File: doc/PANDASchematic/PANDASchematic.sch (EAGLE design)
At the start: 11 parts, among them IC1 74LS595N, U1 ELECTRIC_IMP

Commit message: Laid out schematic and state transfers
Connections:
- net GND: now also IC1A.G
- net VDD: now also LCD1.VDD
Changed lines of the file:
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@@
 <part name="SUPPLY8" library="supply2" deviceset="GND" device=""/>
 <part name="SUPPLY9" library="supply2" deviceset="GND" device=""/>
+<part name="SUPPLY10" library="supply2" deviceset="GND" device=""/>
+<part name="SUPPLY11" library="SparkFun-Aesthetics" deviceset="VDD" device=""/>
 </parts>
 <sheets>
@@
 <instance part="SUPPLY8" gate="GND" x="76.2" y="68.58"/>
 <instance part="SUPPLY9" gate="GND" x="38.1" y="68.58"/>
+<instance part="SUPPLY10" gate="GND" x="104.14" y="50.8"/>
+<instance part="SUPPLY11" gate="VDD" x="35.56" y="40.64"/>
 </instances>
 <busses>
@@
 <pinref part="SUPPLY9" gate="GND" pin="GND"/>
 </segment>
+<segment>
+<pinref part="IC1" gate="A" pin="G"/>
+<pinref part="SUPPLY10" gate="GND" pin="GND"/>
+<wire x1="104.14" y1="53.34" x2="101.6" y2="53.34" width="0.1524" layer="91"/>
+</segment>
 </net>
 <net name="VDD" class="0">
@@
 <wire x1="104.14" y1="38.1" x2="101.6" y2="38.1" width="0.1524" layer="91"/>
 </segment>
+<segment>
+<pinref part="LCD1" gate="G$1" pin="VDD"/>
+<pinref part="SUPPLY11" gate="VDD" pin="VDD"/>
+<wire x1="35.56" y1="40.64" x2="33.02" y2="40.64" width="0.1524" layer="91"/>
+</segment>
 </net>

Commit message: Updated schematic to match soldered circuit
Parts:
- removed R2: 68Ω, SparkFun-Passives:RESISTORAXIAL-0.3
- added T1: 2N2222, adafruit:2N2222
- LED1, LED2: value TLUV5300 -> LTL-30EFJ
- R4, R5: value 47Ω -> 100Ω
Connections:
- net GND: now also T1.E; no longer R2.2
- net N$10: now also IC1A.QG, LED2.AG; no longer IC1A.QD, LED1.AO
- net N$11: now also IC1A.QF, LED1.AO; no longer IC1A.QE, LED2.AG
- net N$12: now also IC1A.QE, LED1.AG; no longer IC1A.QF, LED2.AO
- net N$13: now also T1.B, U1.1(CLK2/CTS1/TX3/SCL2); no longer R2.1, SG1.2
- net N$3: now also SG1.2, T1.C; no longer SG1.1, U1.1(CLK2/CTS1/TX3/SCL2)
- net N$7: now also IC1A.QC; no longer IC1A.QA
- net N$9: now also IC1A.QH, LED2.AO; no longer IC1A.QC, LED1.AG
- net VDD: now also SG1.1
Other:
- moved on the sheet: SG1
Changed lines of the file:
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@@
 <layer number="230" name="230bmp" color="7" fill="1" visible="yes" active="yes"/>
 <layer number="231" name="231bmp" color="7" fill="1" visible="yes" active="yes"/>
+<layer number="232" name="Eagle3D_PG2" color="7" fill="1" visible="no" active="no"/>
+<layer number="233" name="Eagle3D_PG3" color="7" fill="1" visible="no" active="no"/>
 <layer number="248" name="Housing" color="7" fill="1" visible="yes" active="yes"/>
 <layer number="249" name="Edge" color="7" fill="1" visible="yes" active="yes"/>
@@
 <parts>
 <part name="U1" library="SparkFun-RF" deviceset="ELECTRIC_IMP" device=""/>
-<part name="LED1" library="led" deviceset="TLUV5300" device=""/>
-<part name="LED2" library="led" deviceset="TLUV5300" device=""/>
+<part name="LED1" library="led" deviceset="TLUV5300" device="" value="LTL-30EFJ"/>
+<part name="LED2" library="led" deviceset="TLUV5300" device="" value="LTL-30EFJ"/>
 <part name="LCD1" library="lph-7366" deviceset="LPH-7366" device=""/>
 <part name="IC1" library="74xx-us" deviceset="74*595" device="N" technology="LS"/>
 <part name="SG1" library="SparkFun-Electromechanical" deviceset="BUZZER" device="NS"/>
 <part name="R1" library="SparkFun-Sensors" deviceset="PHOTOCELL" device="PTH"/>
-<part name="R2" library="SparkFun-Passives" deviceset="RESISTOR" device="AXIAL-0.3" value="68Ω"/>
 <part name="R3" library="SparkFun-Passives" deviceset="RESISTOR" device="AXIAL-0.3" value="10kΩ"/>
 <part name="SUPPLY2" library="supply2" deviceset="GND" device=""/>
@@
 <part name="SUPPLY6" library="SparkFun-Aesthetics" deviceset="VDD" device=""/>
 <part name="SUPPLY7" library="SparkFun-Aesthetics" deviceset="VDD" device=""/>
-<part name="R4" library="SparkFun-Passives" deviceset="RESISTOR" device="AXIAL-0.3" value="47Ω"/>
-<part name="R5" library="SparkFun-Passives" deviceset="RESISTOR" device="AXIAL-0.3" value="47Ω"/>
+<part name="R4" library="SparkFun-Passives" deviceset="RESISTOR" device="AXIAL-0.3" value="100Ω"/>
+<part name="R5" library="SparkFun-Passives" deviceset="RESISTOR" device="AXIAL-0.3" value="100Ω"/>
 <part name="SUPPLY8" library="supply2" deviceset="GND" device=""/>
 <part name="SUPPLY9" library="supply2" deviceset="GND" device=""/>
 <part name="SUPPLY10" library="supply2" deviceset="GND" device=""/>
 <part name="SUPPLY11" library="SparkFun-Aesthetics" deviceset="VDD" device=""/>
+<part name="T1" library="adafruit" deviceset="2N2222" device=""/>
+<part name="SUPPLY12" library="SparkFun-Aesthetics" deviceset="VDD" device=""/>
 </parts>
 <sheets>
@@
 <instance part="LCD1" gate="G$1" x="15.24" y="35.56" rot="R180"/>
 <instance part="IC1" gate="A" x="91.44" y="40.64" rot="R180"/>
-<instance part="SG1" gate="G$1" x="121.92" y="40.64"/>
+<instance part="SG1" gate="G$1" x="124.46" y="55.88"/>
 <instance part="R1" gate="G$1" x="73.66" y="5.08" rot="R180"/>
-<instance part="R2" gate="G$1" x="137.16" y="35.56"/>
 <instance part="R3" gate="G$1" x="91.44" y="5.08" rot="R180"/>
 <instance part="SUPPLY2" gate="GND" x="35.56" y="50.8"/>
 <instance part="SUPPLY1" gate="VDD" x="175.26" y="25.4"/>
 <instance part="SUPPLY3" gate="GND" x="175.26" y="7.62"/>
-<instance part="SUPPLY4" gate="GND" x="147.32" y="33.02"/>
+<instance part="SUPPLY4" gate="GND" x="127" y="35.56"/>
 <instance part="SUPPLY5" gate="GND" x="66.04" y="0"/>
 <instance part="SUPPLY6" gate="VDD" x="99.06" y="5.08"/>
 <instance part="SUPPLY7" gate="VDD" x="104.14" y="38.1"/>
 <instance part="R4" gate="G$1" x="43.18" y="71.12" rot="R180"/>
-<instance part="R5" gate="G$1" x="71.12" y="71.12" rot="R180"/>
-<instance part="SUPPLY8" gate="GND" x="76.2" y="68.58"/>
+<instance part="R5" gate="G$1" x="71.12" y="71.12" smashed="yes" rot="R180">
+<attribute name="NAME" x="72.39" y="69.6214" size="1.778" layer="95" rot="R180"/>
+<attribute name="VALUE" x="74.93" y="74.422" size="1.778" layer="96" rot="R180"/>
+</instance>
+<instance part="SUPPLY8" gate="GND" x="76.2" y="68.58" smashed="yes">
+<attribute name="VALUE" x="74.295" y="65.405" size="1.778" layer="96"/>
+</instance>
 <instance part="SUPPLY9" gate="GND" x="38.1" y="68.58"/>
 <instance part="SUPPLY10" gate="GND" x="104.14" y="50.8"/>
 <instance part="SUPPLY11" gate="VDD" x="35.56" y="40.64"/>
+<instance part="T1" gate="G$1" x="124.46" y="45.72" smashed="yes">
+<attribute name="NAME" x="129.54" y="48.26" size="1.778" layer="95"/>
+<attribute name="VALUE" x="129.54" y="45.72" size="1.778" layer="96"/>
+</instance>
+<instance part="SUPPLY12" gate="VDD" x="119.38" y="63.5"/>
 </instances>
 <busses>
@@
 </segment>
 <segment>
-<pinref part="R2" gate="G$1" pin="2"/>
-<pinref part="SUPPLY4" gate="GND" pin="GND"/>
-<wire x1="147.32" y1="35.56" x2="142.24" y2="35.56" width="0.1524" layer="91"/>
-</segment>
-<segment>
 <pinref part="R5" gate="G$1" pin="1"/>
 <pinref part="SUPPLY8" gate="GND" pin="GND"/>
@@
 <wire x1="104.14" y1="53.34" x2="101.6" y2="53.34" width="0.1524" layer="91"/>
 </segment>
+<segment>
+<pinref part="T1" gate="G$1" pin="E"/>
+<pinref part="SUPPLY4" gate="GND" pin="GND"/>
+<wire x1="127" y1="40.64" x2="127" y2="38.1" width="0.1524" layer="91"/>
+</segment>
 </net>
 <net name="VDD" class="0">
@@
 <pinref part="SUPPLY11" gate="VDD" pin="VDD"/>
 <wire x1="35.56" y1="40.64" x2="33.02" y2="40.64" width="0.1524" layer="91"/>
+</segment>
+<segment>
+<pinref part="SUPPLY12" gate="VDD" pin="VDD"/>
+<wire x1="119.38" y1="63.5" x2="119.38" y2="53.34" width="0.1524" layer="91"/>
+<pinref part="SG1" gate="G$1" pin="1"/>
+<wire x1="119.38" y1="53.34" x2="124.46" y2="53.34" width="0.1524" layer="91"/>
 </segment>
 </net>
@@
 </segment>
 </net>
-<net name="N$3" class="0">
-<segment>
-<pinref part="SG1" gate="G$1" pin="1"/>
-<pinref part="U1" gate="G$1" pin="1(CLK2/CTS1/TX3/SCL2)"/>
-<wire x1="121.92" y1="38.1" x2="121.92" y2="25.4" width="0.1524" layer="91"/>
-</segment>
-</net>
-<net name="N$7" class="0">
-<segment>
-<pinref part="LCD1" gate="G$1" pin="/RES"/>
-<pinref part="IC1" gate="A" pin="QA"/>
-<wire x1="33.02" y1="30.48" x2="78.74" y2="30.48" width="0.1524" layer="91"/>
-</segment>
-</net>
 <net name="N$8" class="0">
 <segment>
@@
 <wire x1="48.26" y1="22.86" x2="48.26" y2="33.02" width="0.1524" layer="91"/>
 <pinref part="IC1" gate="A" pin="QB"/>
-<wire x1="48.26" y1="33.02" x2="78.74" y2="33.02" width="0.1524" layer="91"/>
-</segment>
-</net>
-<net name="N$9" class="0">
-<segment>
-<pinref part="IC1" gate="A" pin="QC"/>
-<pinref part="LED1" gate="G$1" pin="AG"/>
-<wire x1="78.74" y1="35.56" x2="40.64" y2="35.56" width="0.1524" layer="91"/>
-<wire x1="40.64" y1="35.56" x2="40.64" y2="60.96" width="0.1524" layer="91"/>
-</segment>
-</net>
-<net name="N$10" class="0">
-<segment>
-<pinref part="LED1" gate="G$1" pin="AO"/>
-<wire x1="55.88" y1="60.96" x2="55.88" y2="38.1" width="0.1524" layer="91"/>
-<pinref part="IC1" gate="A" pin="QD"/>
-<wire x1="55.88" y1="38.1" x2="78.74" y2="38.1" width="0.1524" layer="91"/>
-</segment>
-</net>
-<net name="N$11" class="0">
-<segment>
-<pinref part="LED2" gate="G$1" pin="AG"/>
-<wire x1="58.42" y1="60.96" x2="58.42" y2="40.64" width="0.1524" layer="91"/>
-<pinref part="IC1" gate="A" pin="QE"/>
-<wire x1="58.42" y1="40.64" x2="78.74" y2="40.64" width="0.1524" layer="91"/>
-</segment>
-</net>
-<net name="N$12" class="0">
-<segment>
-<pinref part="LED2" gate="G$1" pin="AO"/>
-<wire x1="73.66" y1="60.96" x2="73.66" y2="43.18" width="0.1524" layer="91"/>
-<pinref part="IC1" gate="A" pin="QF"/>
-<wire x1="73.66" y1="43.18" x2="78.74" y2="43.18" width="0.1524" layer="91"/>
-</segment>
-</net>
-<net name="N$13" class="0">
-<segment>
-<pinref part="SG1" gate="G$1" pin="2"/>
-<pinref part="R2" gate="G$1" pin="1"/>
-<wire x1="132.08" y1="35.56" x2="124.46" y2="35.56" width="0.1524" layer="91"/>
-<wire x1="124.46" y1="35.56" x2="124.46" y2="38.1" width="0.1524" layer="91"/>
+<wire x1="78.74" y1="33.02" x2="48.26" y2="33.02" width="0.1524" layer="91"/>
 </segment>
 </net>
@@
 </segment>
 </net>
+<net name="N$3" class="0">
+<segment>
+<pinref part="SG1" gate="G$1" pin="2"/>
+<pinref part="T1" gate="G$1" pin="C"/>
+<wire x1="127" y1="53.34" x2="127" y2="50.8" width="0.1524" layer="91"/>
+</segment>
+</net>
+<net name="N$13" class="0">
+<segment>
+<pinref part="T1" gate="G$1" pin="B"/>
+<pinref part="U1" gate="G$1" pin="1(CLK2/CTS1/TX3/SCL2)"/>
+<wire x1="121.92" y1="45.72" x2="121.92" y2="25.4" width="0.1524" layer="91"/>
+</segment>
+</net>
+<net name="N$7" class="0">
+<segment>
+<pinref part="LCD1" gate="G$1" pin="/RES"/>
+<wire x1="33.02" y1="30.48" x2="45.72" y2="30.48" width="0.1524" layer="91"/>
+<wire x1="45.72" y1="30.48" x2="45.72" y2="35.56" width="0.1524" layer="91"/>
+<pinref part="IC1" gate="A" pin="QC"/>
+<wire x1="45.72" y1="35.56" x2="78.74" y2="35.56" width="0.1524" layer="91"/>
+</segment>
+</net>
+<net name="N$9" class="0">
+<segment>
+<pinref part="LED2" gate="G$1" pin="AO"/>
+<wire x1="73.66" y1="60.96" x2="73.66" y2="48.26" width="0.1524" layer="91"/>
+<pinref part="IC1" gate="A" pin="QH"/>
+<wire x1="73.66" y1="48.26" x2="78.74" y2="48.26" width="0.1524" layer="91"/>
+</segment>
+</net>
+<net name="N$10" class="0">
+<segment>
+<pinref part="LED2" gate="G$1" pin="AG"/>
+<wire x1="58.42" y1="60.96" x2="58.42" y2="45.72" width="0.1524" layer="91"/>
+<pinref part="IC1" gate="A" pin="QG"/>
+<wire x1="58.42" y1="45.72" x2="78.74" y2="45.72" width="0.1524" layer="91"/>
+</segment>
+</net>
+<net name="N$11" class="0">
+<segment>
+<pinref part="LED1" gate="G$1" pin="AO"/>
+<wire x1="55.88" y1="60.96" x2="55.88" y2="43.18" width="0.1524" layer="91"/>
+<pinref part="IC1" gate="A" pin="QF"/>
+<wire x1="55.88" y1="43.18" x2="78.74" y2="43.18" width="0.1524" layer="91"/>
+</segment>
+</net>
+<net name="N$12" class="0">
+<segment>
+<pinref part="IC1" gate="A" pin="QE"/>
+<wire x1="40.64" y1="40.64" x2="78.74" y2="40.64" width="0.1524" layer="91"/>
+<pinref part="LED1" gate="G$1" pin="AG"/>
+<wire x1="40.64" y1="60.96" x2="40.64" y2="40.64" width="0.1524" layer="91"/>
+</segment>
+</net>

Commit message: Updated documentation, added series resistors to SCL/MOSI lines
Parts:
- added R2, R6: 68Ω, SparkFun-Passives:RESISTORAXIAL-0.3
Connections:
- new net N$16: LCD1.SCLK, R2.2
- new net N$17: LCD1.SDIN, R6.2
- net N$1: now also R6.1; no longer LCD1.SDIN
- net N$2: now also R2.1; no longer LCD1.SCLK
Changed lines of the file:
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@@
 <part name="T1" library="adafruit" deviceset="2N2222" device=""/>
 <part name="SUPPLY12" library="SparkFun-Aesthetics" deviceset="VDD" device=""/>
+<part name="R2" library="SparkFun-Passives" deviceset="RESISTOR" device="AXIAL-0.3" value="68Ω"/>
+<part name="R6" library="SparkFun-Passives" deviceset="RESISTOR" device="AXIAL-0.3" value="68Ω"/>
 </parts>
 <sheets>
@@
 </instance>
 <instance part="SUPPLY12" gate="VDD" x="119.38" y="63.5"/>
+<instance part="R2" gate="G$1" x="58.42" y="20.32" rot="R180"/>
+<instance part="R6" gate="G$1" x="71.12" y="17.78" rot="R180"/>
 </instances>
 <busses>
@@
 <net name="N$2" class="0">
 <segment>
-<pinref part="LCD1" gate="G$1" pin="SCLK"/>
 <pinref part="U1" gate="G$1" pin="5(SCLK1/SCLK2/TX2)"/>
-<wire x1="33.02" y1="20.32" x2="106.68" y2="20.32" width="0.1524" layer="91"/>
 <pinref part="IC1" gate="A" pin="SCK"/>
 <wire x1="106.68" y1="20.32" x2="121.92" y2="20.32" width="0.1524" layer="91"/>
 <wire x1="101.6" y1="35.56" x2="106.68" y2="35.56" width="0.1524" layer="91"/>
 <wire x1="106.68" y1="35.56" x2="106.68" y2="20.32" width="0.1524" layer="91"/>
+<pinref part="R2" gate="G$1" pin="1"/>
+<wire x1="63.5" y1="20.32" x2="106.68" y2="20.32" width="0.1524" layer="91"/>
 <junction x="106.68" y="20.32"/>
 </segment>
@@
 <pinref part="IC1" gate="A" pin="SER"/>
 <wire x1="101.6" y1="30.48" x2="104.14" y2="30.48" width="0.1524" layer="91"/>
-<pinref part="LCD1" gate="G$1" pin="SDIN"/>
 <pinref part="U1" gate="G$1" pin="7(MOSI1/MISO2/RX2)"/>
-<wire x1="33.02" y1="17.78" x2="104.14" y2="17.78" width="0.1524" layer="91"/>
 <wire x1="104.14" y1="17.78" x2="121.92" y2="17.78" width="0.1524" layer="91"/>
 <wire x1="104.14" y1="30.48" x2="104.14" y2="17.78" width="0.1524" layer="91"/>
+<pinref part="R6" gate="G$1" pin="1"/>
+<wire x1="76.2" y1="17.78" x2="104.14" y2="17.78" width="0.1524" layer="91"/>
 <junction x="104.14" y="17.78"/>
 </segment>
@@
 </segment>
 </net>
+<net name="N$16" class="0">
+<segment>
+<pinref part="LCD1" gate="G$1" pin="SCLK"/>
+<pinref part="R2" gate="G$1" pin="2"/>
+<wire x1="33.02" y1="20.32" x2="53.34" y2="20.32" width="0.1524" layer="91"/>
+</segment>
+</net>
+<net name="N$17" class="0">
+<segment>
+<pinref part="LCD1" gate="G$1" pin="SDIN"/>
+<pinref part="R6" gate="G$1" pin="2"/>
+<wire x1="33.02" y1="17.78" x2="66.04" y2="17.78" width="0.1524" layer="91"/>
+</segment>
+</net>

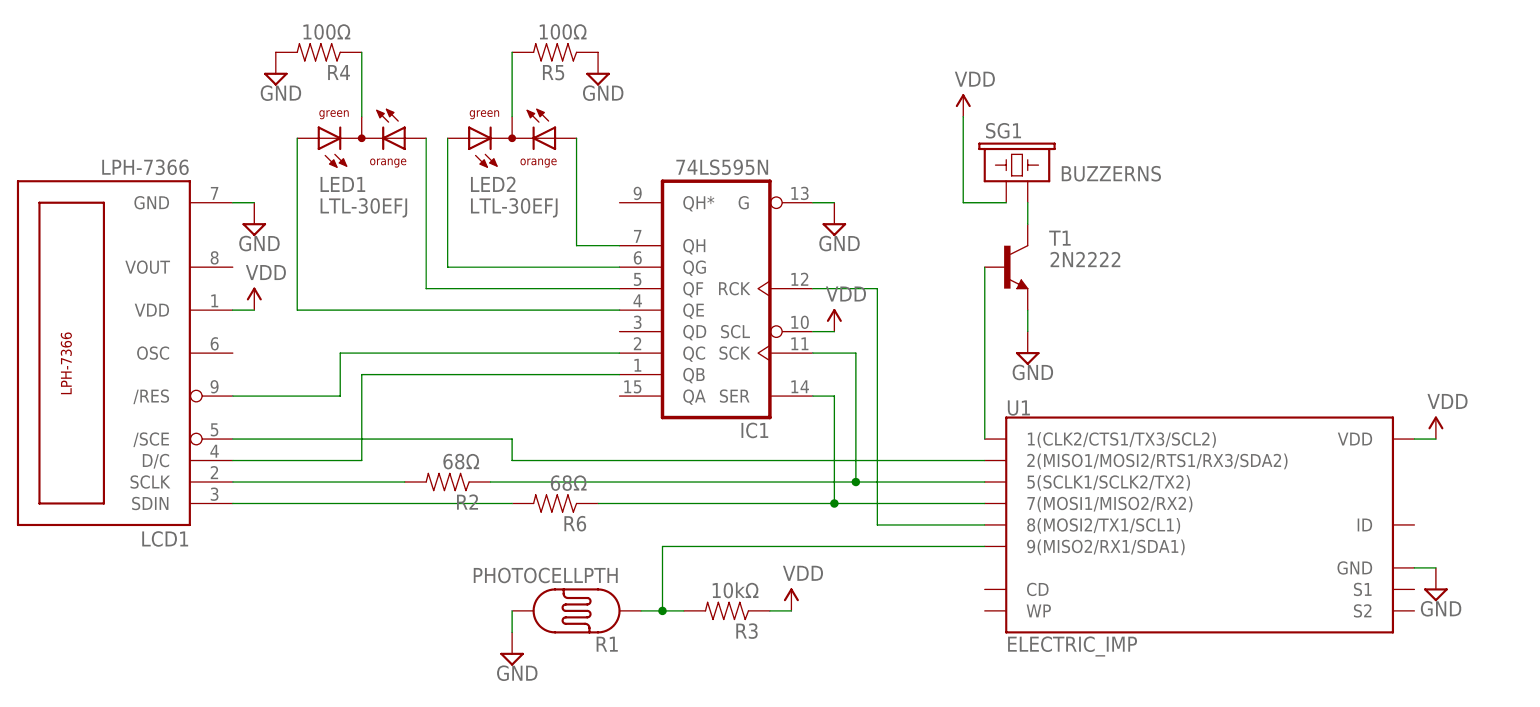
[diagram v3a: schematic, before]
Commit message: Updated schematic to 3 LEDs
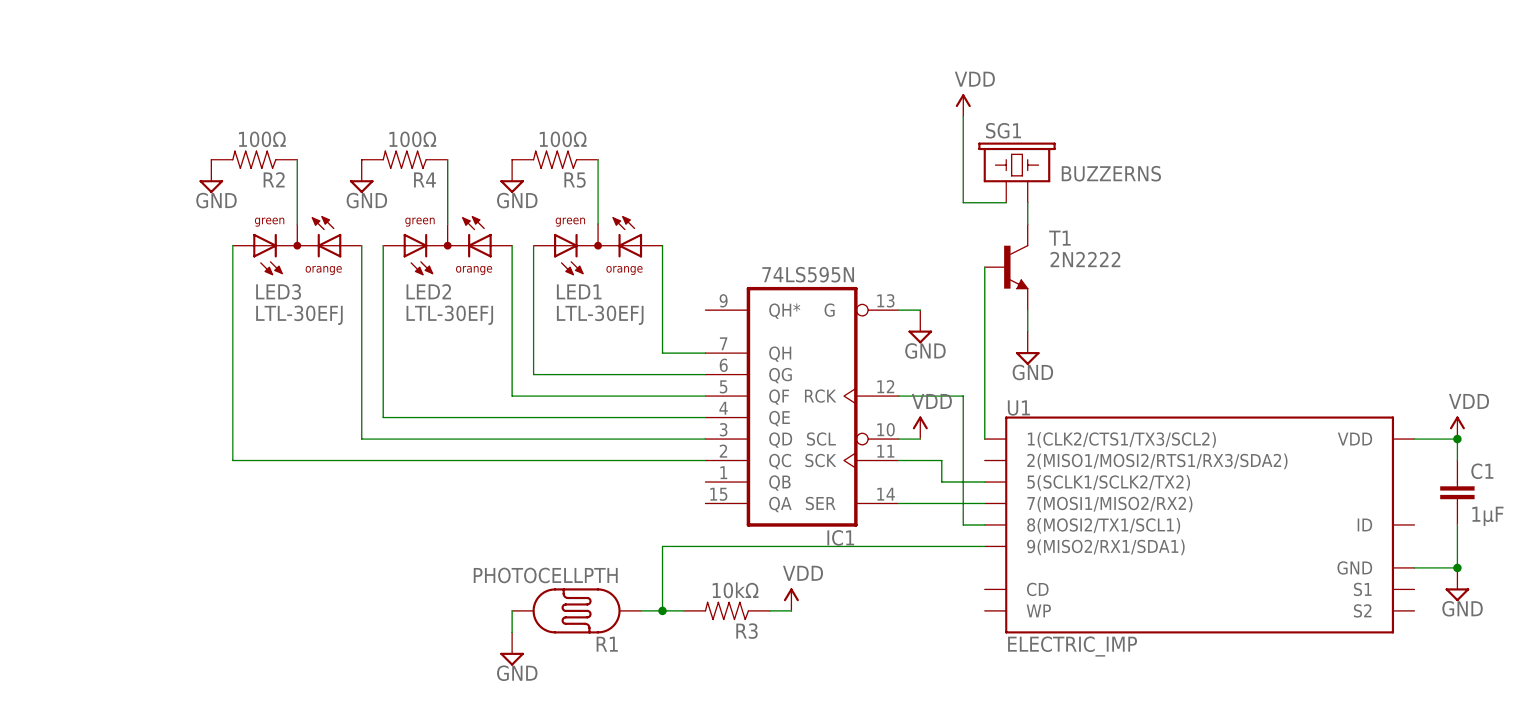
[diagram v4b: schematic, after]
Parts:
- removed LCD1: LPH-7366, lph-7366:LPH-7366
- removed R6: 68Ω, SparkFun-Passives:RESISTORAXIAL-0.3
- added C1: 1µF, SparkFun-Capacitors:CAPPTH
- added LED3: LTL-30EFJ, led:TLUV5300
- R2: value 68Ω -> 100Ω
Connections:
- removed net N$16: LCD1.SCLK, R2.2
- removed net N$17: LCD1.SDIN, R6.2
- net GND: now also C1.2, R2.2, R5.2; no longer LCD1.GND, R5.1
- net N$1: no longer R6.1
- net N$10: now also LED1.AG; no longer LED2.AG
- net N$11: now also LED2.AO; no longer LED1.AO
- net N$12: now also LED2.AG; no longer LED1.AG
- net N$14: now also LED2.CC; no longer LED1.CC
- net N$15: now also LED1.CC, R5.1; no longer LED2.CC, R5.2
- net N$2: no longer R2.1
- net N$4: now also IC1A.QD, LED3.AO; no longer LCD1./SCE, U1.2(MISO1/MOSI2/RTS1/RX3/SDA2)
- net N$7: now also LED3.AG; no longer LCD1./RES
- net N$8: now also LED3.CC, R2.1; no longer IC1A.QB, LCD1.D/C
- net N$9: now also LED1.AO; no longer LED2.AO
- net VDD: now also C1.1; no longer LCD1.VDD
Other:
- moved on the sheet: IC1, LED1, LED2, R2, R4, R5
